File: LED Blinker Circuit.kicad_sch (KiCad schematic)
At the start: 8 parts, among them J1 Conn_01x02_Pin, U1 NE555D

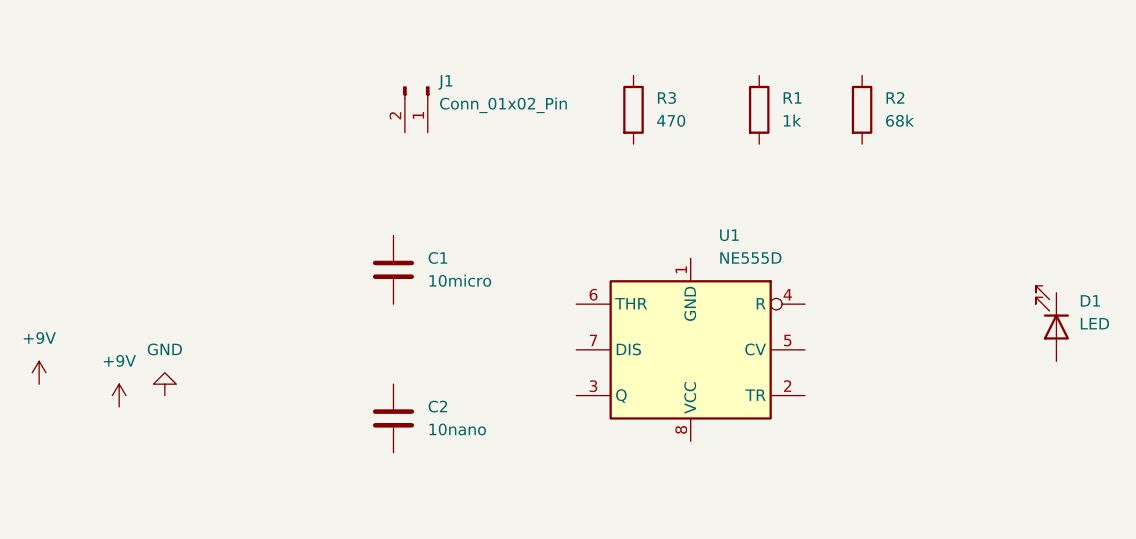
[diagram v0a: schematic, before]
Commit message: schematic update
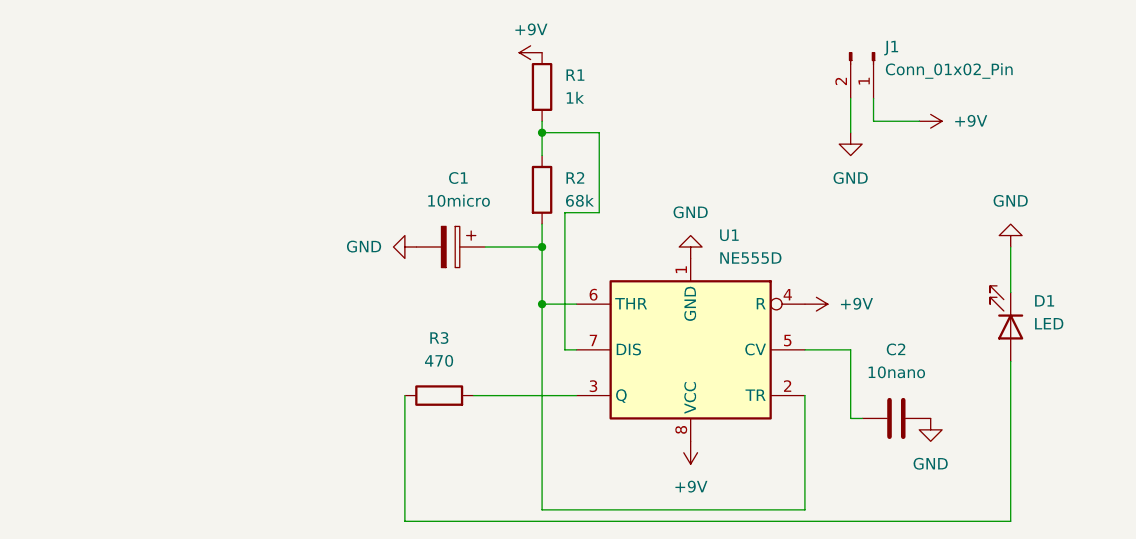
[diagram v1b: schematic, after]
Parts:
- removed C1: 10micro, symbol Device:C
- added C1: 10micro, symbol Device:C_Polarized
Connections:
- net +9V: now also J1.1 (Pin_1), R1.1, U1.4 (R), U1.8 (VCC)
- net GND: now also C2.2, D1.1 (K), J1.2 (Pin_2), U1.1 (GND), C1.2
- net at R1.2: now also R2.1, U1.7 (DIS)
- net at C2.1: now also U1.5 (CV)
- net at R3.1: now also D1.2 (A)
- net at R3.2: now also U1.3 (Q)
- net at R2.2: now also U1.2 (TR), U1.6 (THR), C1.1
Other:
- moved on the sheet: C2, D1, J1, R1, R2, R3

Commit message: breadboard version
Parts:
- C1: value 10micro -> 10u; footprint (none) -> Capacitor_THT:CP_Axial_L10.0mm_D6.0mm_P15.00mm_Horizontal
- C2: value 10nano -> 10n; footprint (none) -> Capacitor_THT:CP_Axial_L10.0mm_D4.5mm_P15.00mm_Horizontal
- D1: footprint (none) -> LED_THT:LED_D3.0mm_Horizontal_O1.27mm_Z2.0mm_Clear
- J1: footprint (none) -> Connector_PinSocket_2.54mm:PinSocket_1x01_P2.54mm_Horizontal
- R1: footprint (none) -> Resistor_THT:R_Axial_DIN0204_L3.6mm_D1.6mm_P1.90mm_Vertical
- R2: footprint (none) -> Resistor_THT:R_Axial_DIN0204_L3.6mm_D1.6mm_P5.08mm_Horizontal
- R3: footprint (none) -> Resistor_THT:R_Axial_DIN0204_L3.6mm_D1.6mm_P2.54mm_Vertical
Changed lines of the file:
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@@
 			)
 		)
-		(property "Footprint" ""
+		(property "Footprint" "Resistor_THT:R_Axial_DIN0204_L3.6mm_D1.6mm_P1.90mm_Vertical"
 			(at 127.762 63.5 90)
 			(effects
@@
 			)
 		)
-		(property "Value" "10nano"
+		(property "Value" "10n"
 			(at 168.91 95.25 90)
 			(effects
@@
 			)
 		)
-		(property "Footprint" ""
+		(property "Footprint" "Capacitor_THT:CP_Axial_L10.0mm_D4.5mm_P15.00mm_Horizontal"
 			(at 172.72 99.3648 0)
 			(effects
@@
 			)
 		)
-		(property "Footprint" ""
+		(property "Footprint" "Resistor_THT:R_Axial_DIN0204_L3.6mm_D1.6mm_P2.54mm_Vertical"
 			(at 118.11 99.568 90)
 			(effects
@@
 			)
 		)
-		(property "Footprint" ""
+		(property "Footprint" "Resistor_THT:R_Axial_DIN0204_L3.6mm_D1.6mm_P5.08mm_Horizontal"
 			(at 127.762 74.93 90)
 			(effects
@@
 			)
 		)
-		(property "Value" "10micro"
+		(property "Value" "10u"
 			(at 120.269 76.2 90)
 			(effects
@@
 			)
 		)
-		(property "Footprint" ""
+		(property "Footprint" "Capacitor_THT:CP_Axial_L10.0mm_D6.0mm_P15.00mm_Horizontal"
 			(at 115.57 82.2452 0)
 			(effects
@@
 			)
 		)
-		(property "Footprint" ""
+		(property "Footprint" "Connector_PinSocket_2.54mm:PinSocket_1x01_P2.54mm_Horizontal"
 			(at 166.37 59.69 0)
 			(effects
@@
 			)
 		)
-		(property "Footprint" ""
+		(property "Footprint" "LED_THT:LED_D3.0mm_Horizontal_O1.27mm_Z2.0mm_Clear"
 			(at 181.61 90.17 0)
 			(effects
